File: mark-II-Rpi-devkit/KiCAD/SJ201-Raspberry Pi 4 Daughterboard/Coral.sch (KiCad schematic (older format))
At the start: 9 parts, among them U2 CoralTPU

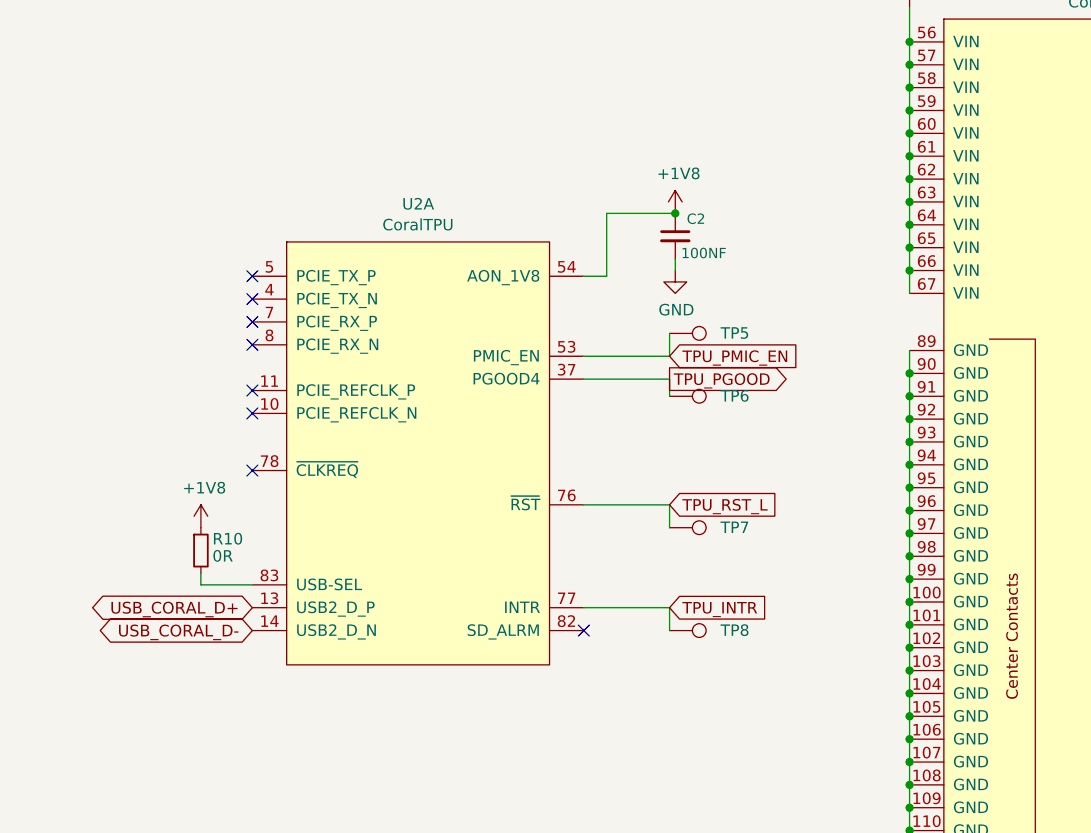
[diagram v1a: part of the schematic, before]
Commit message: SJ-201-R6 for FAB - removed buffer IC
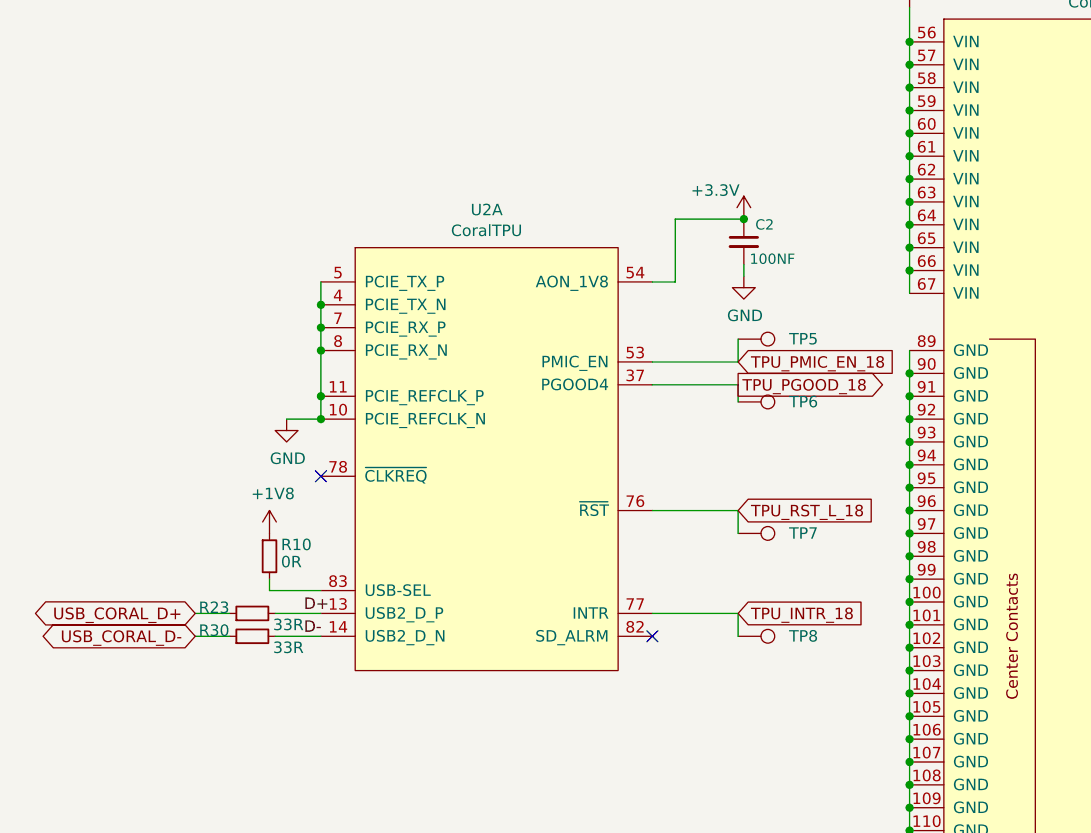
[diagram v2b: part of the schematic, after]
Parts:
- added R23, R30: 33R, Resistor_SMD:R_0402_1005Metric, symbol Device:R_Small
- TP5, TP6, TP7, TP8: footprint TestPoint:TestPoint_Pad_D1.0mm -> TestPoint:TestPoint_Pad_D2.0mm
- U2: Link (none) -> https://www.mouser.com/ProductDetail/Coral/G313-06329-00/; MPN (none) -> G313-06329-00
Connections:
- net +1V8: no longer C2.1, U2.54 (AON_1V8)
- net +3V3: now also C2.1, U2.54 (AON_1V8)
- net GND: now also U2.10 (PCIE_REFCLK_N), U2.11 (PCIE_REFCLK_P), U2.4 (PCIE_TX_N), U2.5 (PCIE_TX_P), U2.7 (PCIE_RX_P), U2.8 (PCIE_RX_N)
- net USB_CORAL_D+: now also R23.1; no longer U2.13 (USB2_D_P)
- net USB_CORAL_D-: now also R30.1; no longer U2.14 (USB2_D_N)
- net TPU_INTR renamed TPU_INTR_18
- net TPU_PGOOD renamed TPU_PGOOD_18
- net TPU_PMIC_EN renamed TPU_PMIC_EN_18
- net TPU_RST_L renamed TPU_RST_L_18
- new net D+: R23.2, U2.13 (USB2_D_P)
- new net D-: R30.2, U2.14 (USB2_D_N)
- no-connect marks 8 -> 2
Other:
- moved on the sheet: C2, R10, TP5, TP6, TP7, TP8, U2A

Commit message: Updated files for R6 v2
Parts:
- C2, C9: value 100NF -> 100NF-DNP; LCSC C1525 -> C1525-DNP; MPN CC0402KRX7R8BB104 -> CC0402KRX7R8BB104-DNP; SKU 302010024 -> 302010024-DNP
- C65: value 10UF -> 10UF-DNP; LCSC C15525 -> C15525-DNP; MPN CC0402MRX5R5BB106 -> CC0402MRX5R5BB106-DNP; SKU 302010053 -> 302010053-DNP
- R10: value 0R -> 0R-DNP; LCSC C21189 -> C21189-DNP; MPN 0603WAF0000T5E -> 0603WAF0000T5E-DNP; Tempo RC0603JR-070RL -> RC0603JR-070RL-DNP
- R23, R30: value 33R -> 33R-DNP; LCSC C25105 -> C25105-DNP; MPN 0402WGF330JTCE -> 0402WGF330JTCE-DNP
- U2: value CoralTPU -> CoralTPU-DNP; MPN G313-06329-00 -> G313-06329-00-DNP
- U2: value CoralTPU -> CoralTPU-DNP
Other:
- moved on the sheet: R23, R30, TP5, TP6, TP7, TP8

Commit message: Removed unused files, cleaned up directory, remove SJ202
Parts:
- U2: footprint user:CoralTPU -> CoralTPU:CoralTPU; symbol user:CoralTPU -> CoralTPU:CoralTPU
- U2: footprint user:CoralTPU -> CoralTPU:CoralTPU; symbol user:CoralTPU -> Mycroft:CoralTPU
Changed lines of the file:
@@
 	1825 3775 1825 3875
 $Comp
-L user:CoralTPU U2
+L Mycroft:CoralTPU U2
 U 2 1 5F9D96B1
 P 5200 2075
 F 0 "U2" H 5250 2190 50  0000 C CNN
 F 1 "CoralTPU-DNP" H 5250 2099 50  0000 C CNN
-F 2 "user:CoralTPU" H 5200 2075 50  0001 C CNN
+F 2 "CoralTPU:CoralTPU" H 5200 2075 50  0001 C CNN
 F 3 "https://coral.ai/static/files/Coral-Accelerator-Module-datasheet.pdf" H 5200 2075 50  0001 C CNN
 	2    5200 2075
@@
 $EndComp
 $Comp
-L user:CoralTPU U2
+L CoralTPU:CoralTPU U2
 U 1 1 5F9D6A2B
 P 2625 3125
 F 0 "U2" H 2550 3290 50  0000 C CNN
 F 1 "CoralTPU-DNP" H 2550 3199 50  0000 C CNN
-F 2 "user:CoralTPU" H 2625 3125 50  0001 C CNN
+F 2 "CoralTPU:CoralTPU" H 2625 3125 50  0001 C CNN
 F 3 "https://coral.ai/static/files/Coral-Accelerator-Module-datasheet.pdf" H 2625 3125 50  0001 C CNN
 F 4 "G313-06329-00-DNP" H 2625 3125 50  0001 C CNN "MPN"

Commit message: Update libraries, reorganize files
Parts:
- U2: symbol CoralTPU:CoralTPU -> Mycroft:CoralTPU
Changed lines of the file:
@@
 $EndComp
 $Comp
-L CoralTPU:CoralTPU U2
+L Mycroft:CoralTPU U2
 U 1 1 5F9D6A2B
 P 2625 3125
+AR Path="/5F9D6A2B" Ref="U2"  Part="1"
+AR Path="/5F9CAA4F/5F9D6A2B" Ref="U2"  Part="1"
 F 0 "U2" H 2550 3290 50  0000 C CNN
 F 1 "CoralTPU-DNP" H 2550 3199 50  0000 C CNN
